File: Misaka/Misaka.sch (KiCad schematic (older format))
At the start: 4 parts, among them J1 Conn_Coaxial_Power, SW1 SW_DIP_x03, U2 ATmega2560-16AU

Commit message: CH340
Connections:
- net D1 renamed RX0
- net D18 renamed TX1
- net D19 renamed RX1
- net D2 renamed TX0
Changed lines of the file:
@@
 $Descr A4 11693 8268
 encoding utf-8
-Sheet 1 4
+Sheet 1 5
 Title ""
 Date ""
@@
 D50
 Text Label 5100 5300 0    50   ~ 0
-D1
+RX0
 Text Label 5100 5400 0    50   ~ 0
-D2
+TX0
 $Comp
 L Connector:Conn_Coaxial_Power J1
@@
 MS3
 $Comp
+L power:GND #PWR0127
+U 1 1 5E64EFCB
+P 7950 2750
+F 0 "#PWR0127" H 7950 2500 50  0001 C CNN
+F 1 "GND" H 7955 2577 50  0000 C CNN
+F 2 "" H 7950 2750 50  0001 C CNN
+F 3 "" H 7950 2750 50  0001 C CNN
+	1    7950 2750
+	1    0    0    -1
+$EndComp
+$Comp
+L power:+3.3V #PWR0142
+U 1 1 5E64FE9B
+P 8050 1300
+F 0 "#PWR0142" H 8050 1150 50  0001 C CNN
+F 1 "+3.3V" H 8065 1473 50  0000 C CNN
+F 2 "" H 8050 1300 50  0001 C CNN
+F 3 "" H 8050 1300 50  0001 C CNN
+	1    8050 1300
+	1    0    0    -1
+$EndComp
+Wire Wire Line
+	8050 1300 8050 1550
+Text Label 5100 4700 0    50   ~ 0
+TX1
+Text Label 5100 4600 0    50   ~ 0
+RX1
+Text Notes 8450 1000 2    50   ~ 0
+Connect with TX1/RX1
+$Sheet
+S 9800 550  1000 950
+U 5E609346
+F0 "USB-UART" 50
+F1 "CH340.sch" 50
+F2 "TX" I L 9800 1150 50
+F3 "RX" I L 9800 850 50
+$EndSheet
+Wire Wire Line
+	9800 850  9500 850
+Wire Wire Line
+	9800 1150 9500 1150
+Text Label 9500 850  0    50   ~ 0
+TX0
+Text Label 9500 1150 0    50   ~ 0
+RX0
+$Comp
 L dk_RF-Transceiver-Modules:XB24CZ7PIT-004 MOD1
 U 1 1 5E64862E
@@
 	1    0    0    -1
 $EndComp
-$Comp
-L power:GND #PWR0127
-U 1 1 5E64EFCB
-P 7950 2750
-F 0 "#PWR0127" H 7950 2500 50  0001 C CNN
-F 1 "GND" H 7955 2577 50  0000 C CNN
-F 2 "" H 7950 2750 50  0001 C CNN
-F 3 "" H 7950 2750 50  0001 C CNN
-	1    7950 2750
-	1    0    0    -1
-$EndComp
-$Comp
-L power:+3.3V #PWR0142
-U 1 1 5E64FE9B
-P 8050 1300
-F 0 "#PWR0142" H 8050 1150 50  0001 C CNN
-F 1 "+3.3V" H 8065 1473 50  0000 C CNN
-F 2 "" H 8050 1300 50  0001 C CNN
-F 3 "" H 8050 1300 50  0001 C CNN
-	1    8050 1300
-	1    0    0    -1
-$EndComp
-Wire Wire Line
-	8050 1300 8050 1550
-Text Label 5100 4700 0    50   ~ 0
-D18
-Text Label 5100 4600 0    50   ~ 0
-D19
+Text Label 7350 1750 2    50   ~ 0
+TX1
 Text Label 8750 1750 0    50   ~ 0
-D19
-Text Label 7350 1750 2    50   ~ 0
-D18
-Text Notes 8450 1000 2    50   ~ 0
-Connect with TX1/RX1
+RX1
 $EndSCHEMATC

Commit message: CH340C
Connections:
- net +5V: now also U2.100 (AVCC)
- net RESET: now reaches U2.30 (~RESET)
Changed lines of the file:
@@
 	4300 7200 4300 7450
 Wire Wire Line
-	4300 1400 4300 1300
+	4300 1400 4300 1350
 Wire Wire Line
 	9750 3150 9500 3150
@@
 Connect with TX1/RX1
 $Sheet
-S 9800 550  1000 950
+S 9750 550  1000 950
 U 5E609346
 F0 "USB-UART" 50
 F1 "CH340.sch" 50
-F2 "TX" I L 9800 1150 50
-F3 "RX" I L 9800 850 50
+F2 "TX" O L 9750 750 50
+F3 "RX" I L 9750 1250 50
+F4 "RESET" O L 9750 1000 50
 $EndSheet
 Wire Wire Line
-	9800 850  9500 850
-Wire Wire Line
-	9800 1150 9500 1150
-Text Label 9500 850  0    50   ~ 0
+	9750 750  9500 750
+Wire Wire Line
+	9750 1250 9500 1250
+Text Label 9500 750  0    50   ~ 0
 TX0
-Text Label 9500 1150 0    50   ~ 0
+Text Label 9500 1250 0    50   ~ 0
 RX0
 $Comp
@@
 Text Label 8750 1750 0    50   ~ 0
 RX1
+Wire Wire Line
+	9750 1000 9500 1000
+Text Label 9500 1000 0    50   ~ 0
+RESET
+Text Label 3500 1700 2    50   ~ 0
+RESET
+Wire Wire Line
+	4300 1350 4400 1350
+Wire Wire Line
+	4400 1350 4400 1400
+Connection ~ 4300 1350
+Wire Wire Line
+	4300 1350 4300 1300
 $EndSCHEMATC

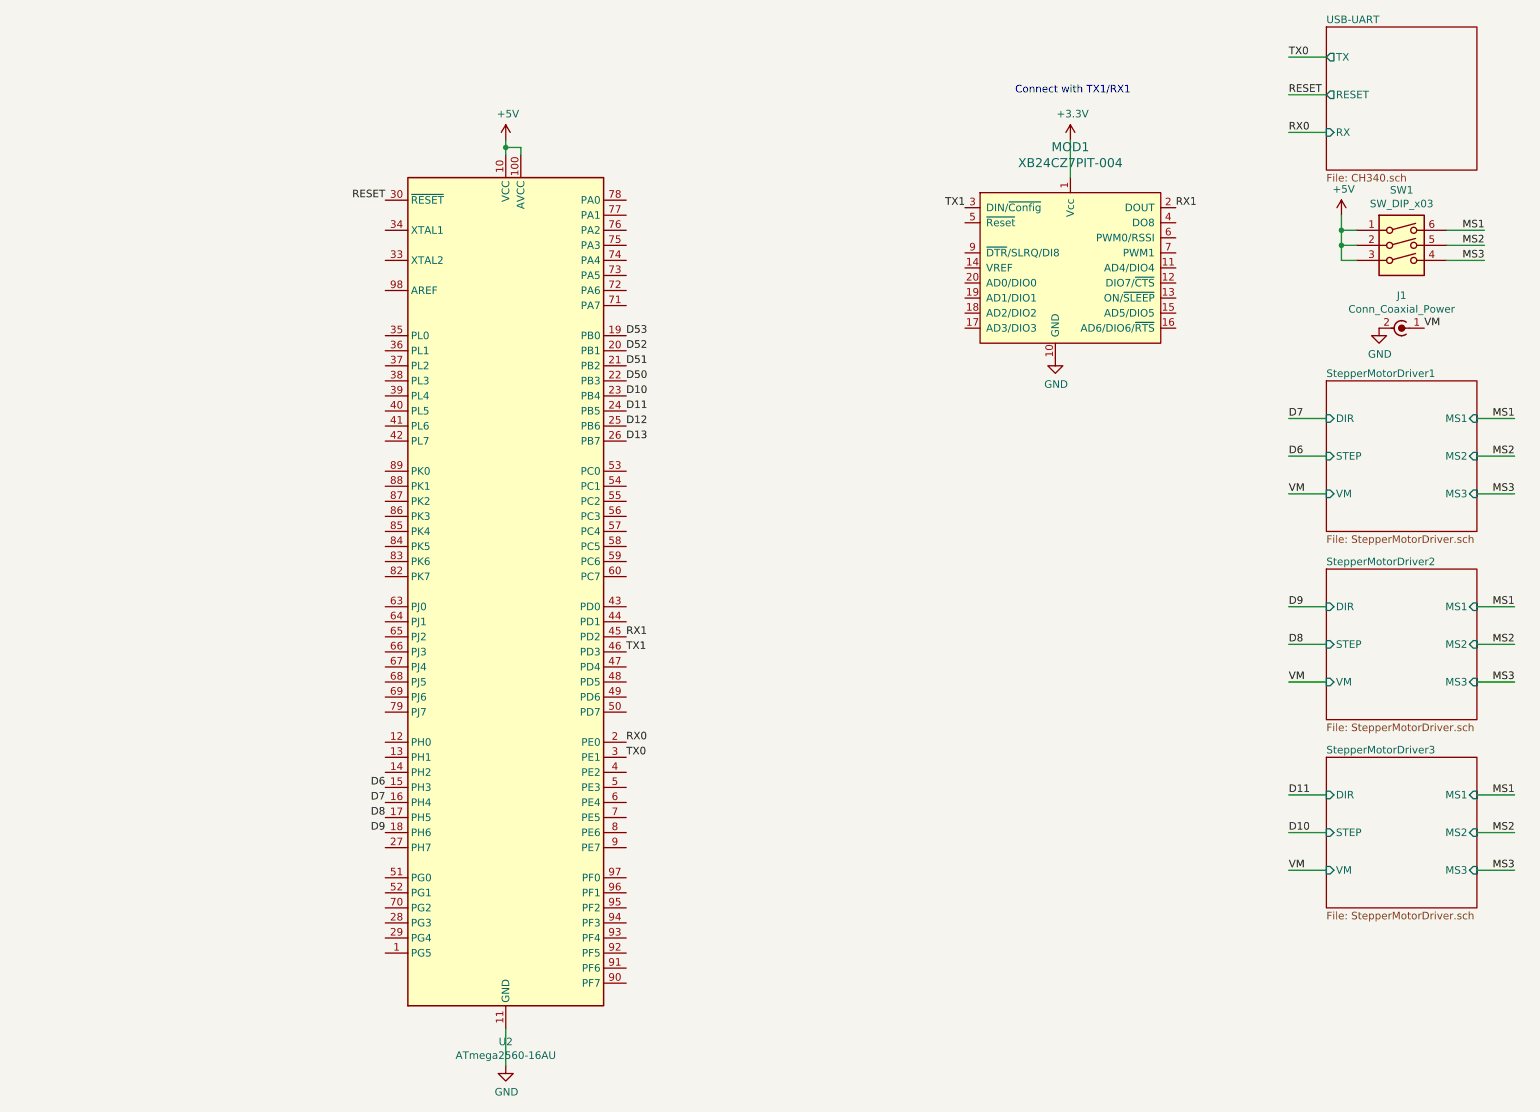
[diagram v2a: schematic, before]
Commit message: MURATA的 CSTLS16M0X51-A0
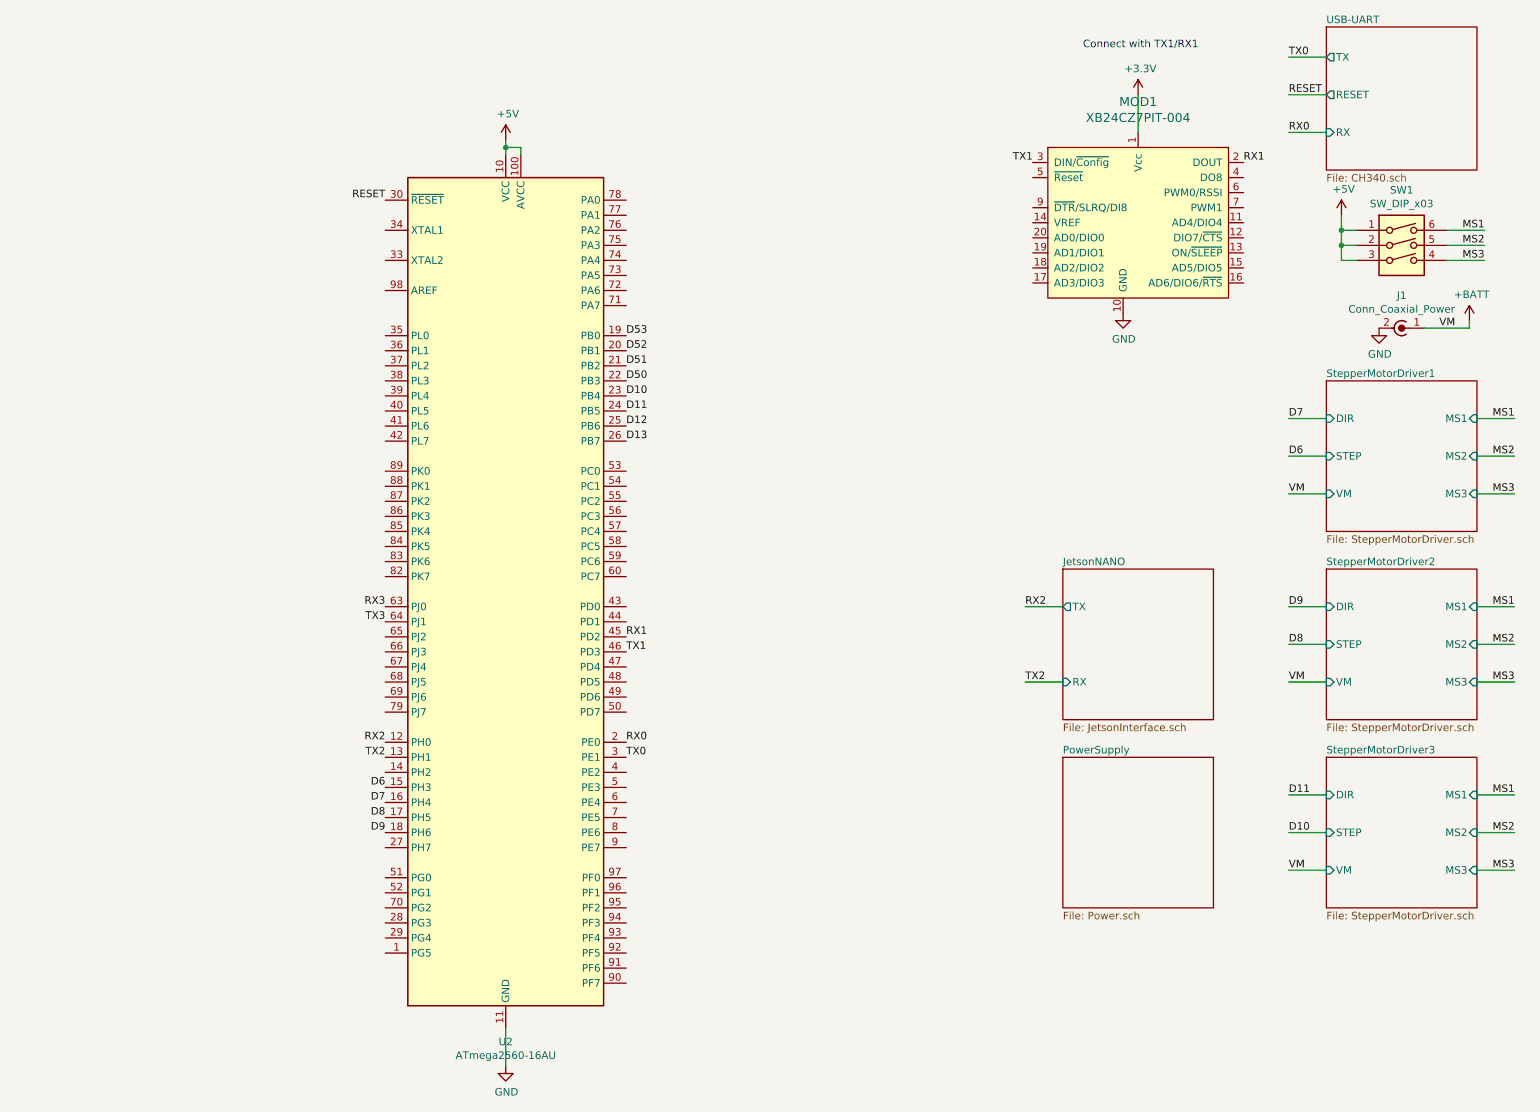
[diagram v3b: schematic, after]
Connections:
- net RX2: now reaches U2.12 (PH0)
- net TX2: now reaches U2.13 (PH1)
- net RX3: now reaches U2.63 (PJ0)
- net TX3: now reaches U2.64 (PJ1)
- net VM renamed +BATT
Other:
- moved on the sheet: MOD1
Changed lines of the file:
@@
 $Descr A4 11693 8268
 encoding utf-8
-Sheet 1 5
+Sheet 1 7
 Title ""
 Date ""
@@
 	0    1    1    0
 $EndComp
-Text Label 10400 2550 0    50   ~ 0
-VM
 $Comp
 L power:GND #PWR0117
@@
 L power:GND #PWR0127
 U 1 1 5E64EFCB
-P 7950 2750
-F 0 "#PWR0127" H 7950 2500 50  0001 C CNN
-F 1 "GND" H 7955 2577 50  0000 C CNN
-F 2 "" H 7950 2750 50  0001 C CNN
-F 3 "" H 7950 2750 50  0001 C CNN
-	1    7950 2750
+P 8400 2450
+F 0 "#PWR0127" H 8400 2200 50  0001 C CNN
+F 1 "GND" H 8405 2277 50  0000 C CNN
+F 2 "" H 8400 2450 50  0001 C CNN
+F 3 "" H 8400 2450 50  0001 C CNN
+	1    8400 2450
 	1    0    0    -1
 $EndComp
@@
 L power:+3.3V #PWR0142
 U 1 1 5E64FE9B
-P 8050 1300
-F 0 "#PWR0142" H 8050 1150 50  0001 C CNN
-F 1 "+3.3V" H 8065 1473 50  0000 C CNN
-F 2 "" H 8050 1300 50  0001 C CNN
-F 3 "" H 8050 1300 50  0001 C CNN
-	1    8050 1300
-	1    0    0    -1
-$EndComp
-Wire Wire Line
-	8050 1300 8050 1550
+P 8500 1000
+F 0 "#PWR0142" H 8500 850 50  0001 C CNN
+F 1 "+3.3V" H 8515 1173 50  0000 C CNN
+F 2 "" H 8500 1000 50  0001 C CNN
+F 3 "" H 8500 1000 50  0001 C CNN
+	1    8500 1000
+	1    0    0    -1
+$EndComp
+Wire Wire Line
+	8500 1000 8500 1250
 Text Label 5100 4700 0    50   ~ 0
 TX1
 Text Label 5100 4600 0    50   ~ 0
 RX1
-Text Notes 8450 1000 2    50   ~ 0
+Text Notes 8900 700  2    50   ~ 0
 Connect with TX1/RX1
+Wire Wire Line
+	9750 750  9500 750
+Wire Wire Line
+	9750 1250 9500 1250
+Text Label 9500 750  0    50   ~ 0
+TX0
+Text Label 9500 1250 0    50   ~ 0
+RX0
+$Comp
+L dk_RF-Transceiver-Modules:XB24CZ7PIT-004 MOD1
+U 1 1 5E64862E
+P 8600 2050
+F 0 "MOD1" H 8500 3053 60  0000 C CNN
+F 1 "XB24CZ7PIT-004" H 8500 2947 60  0000 C CNN
+F 2 "digikey-footprints:XBEE_PRO-20_THT" H 8800 2250 60  0001 L CNN
+F 3 "https://www.digi.com/resources/documentation/digidocs/pdfs/90001500.pdf" H 8800 2350 60  0001 L CNN
+F 4 "602-1557-ND" H 8800 2450 60  0001 L CNN "Digi-Key_PN"
+F 5 "XB24CZ7PIT-004" H 8800 2550 60  0001 L CNN "MPN"
+F 6 "RF/IF and RFID" H 8800 2650 60  0001 L CNN "Category"
+F 7 "RF Transceiver Modules" H 8800 2750 60  0001 L CNN "Family"
+F 8 "https://www.digi.com/resources/documentation/digidocs/pdfs/90001500.pdf" H 8800 2850 60  0001 L CNN "DK_Datasheet_Link"
+F 9 "/product-detail/en/digi-international/XB24CZ7PIT-004/602-1557-ND/5322371" H 8800 2950 60  0001 L CNN "DK_Detail_Page"
+F 10 "RF TXRX MOD 802.15.4 TRACE ANT" H 8800 3050 60  0001 L CNN "Description"
+F 11 "Digi International" H 8800 3150 60  0001 L CNN "Manufacturer"
+F 12 "Active" H 8800 3250 60  0001 L CNN "Status"
+	1    8600 2050
+	1    0    0    -1
+$EndComp
+Text Label 7800 1450 2    50   ~ 0
+TX1
+Text Label 9200 1450 0    50   ~ 0
+RX1
+Wire Wire Line
+	9750 1000 9500 1000
+Text Label 9500 1000 0    50   ~ 0
+RESET
+Text Label 3500 1700 2    50   ~ 0
+RESET
+Wire Wire Line
+	4300 1350 4400 1350
+Wire Wire Line
+	4400 1350 4400 1400
+Connection ~ 4300 1350
+Wire Wire Line
+	4300 1350 4300 1300
+$Sheet
+S 8000 5400 1000 1000
+U 5E6177DE
+F0 "PowerSupply" 50
+F1 "Power.sch" 50
+$EndSheet
+Text Label 3500 4400 2    50   ~ 0
+RX3
+Text Label 3500 4500 2    50   ~ 0
+TX3
+Text Label 3500 5300 2    50   ~ 0
+RX2
+Text Label 3500 5400 2    50   ~ 0
+TX2
+$Sheet
+S 8000 4150 1000 1000
+U 5E61980C
+F0 "JetsonNANO" 50
+F1 "JetsonInterface.sch" 50
+F2 "TX" O L 8000 4400 50
+F3 "RX" I L 8000 4900 50
+$EndSheet
+Wire Wire Line
+	8000 4400 7750 4400
+Wire Wire Line
+	8000 4900 7750 4900
+Text Label 7750 4400 0    50   ~ 0
+RX2
+Text Label 7750 4900 0    50   ~ 0
+TX2
+$Comp
+L power:+BATT #PWR?
+U 1 1 5E62480E
+P 10700 2500
+F 0 "#PWR?" H 10700 2350 50  0001 C CNN
+F 1 "+BATT" H 10715 2673 50  0000 C CNN
+F 2 "" H 10700 2500 50  0001 C CNN
+F 3 "" H 10700 2500 50  0001 C CNN
+	1    10700 2500
+	1    0    0    -1
+$EndComp
 $Sheet
 S 9750 550  1000 950
@@
 $EndSheet
 Wire Wire Line
-	9750 750  9500 750
-Wire Wire Line
-	9750 1250 9500 1250
-Text Label 9500 750  0    50   ~ 0
-TX0
-Text Label 9500 1250 0    50   ~ 0
-RX0
-$Comp
-L dk_RF-Transceiver-Modules:XB24CZ7PIT-004 MOD1
-U 1 1 5E64862E
-P 8150 2350
-F 0 "MOD1" H 8050 3353 60  0000 C CNN
-F 1 "XB24CZ7PIT-004" H 8050 3247 60  0000 C CNN
-F 2 "digikey-footprints:XBEE_PRO-20_THT" H 8350 2550 60  0001 L CNN
-F 3 "https://www.digi.com/resources/documentation/digidocs/pdfs/90001500.pdf" H 8350 2650 60  0001 L CNN
-F 4 "602-1557-ND" H 8350 2750 60  0001 L CNN "Digi-Key_PN"
-F 5 "XB24CZ7PIT-004" H 8350 2850 60  0001 L CNN "MPN"
-F 6 "RF/IF and RFID" H 8350 2950 60  0001 L CNN "Category"
-F 7 "RF Transceiver Modules" H 8350 3050 60  0001 L CNN "Family"
-F 8 "https://www.digi.com/resources/documentation/digidocs/pdfs/90001500.pdf" H 8350 3150 60  0001 L CNN "DK_Datasheet_Link"
-F 9 "/product-detail/en/digi-international/XB24CZ7PIT-004/602-1557-ND/5322371" H 8350 3250 60  0001 L CNN "DK_Detail_Page"
-F 10 "RF TXRX MOD 802.15.4 TRACE ANT" H 8350 3350 60  0001 L CNN "Description"
-F 11 "Digi International" H 8350 3450 60  0001 L CNN "Manufacturer"
-F 12 "Active" H 8350 3550 60  0001 L CNN "Status"
-	1    8150 2350
-	1    0    0    -1
-$EndComp
-Text Label 7350 1750 2    50   ~ 0
-TX1
-Text Label 8750 1750 0    50   ~ 0
-RX1
-Wire Wire Line
-	9750 1000 9500 1000
-Text Label 9500 1000 0    50   ~ 0
-RESET
-Text Label 3500 1700 2    50   ~ 0
-RESET
-Wire Wire Line
-	4300 1350 4400 1350
-Wire Wire Line
-	4400 1350 4400 1400
-Connection ~ 4300 1350
-Wire Wire Line
-	4300 1350 4300 1300
+	10400 2550 10700 2550
+Wire Wire Line
+	10700 2550 10700 2500
+Text Label 10500 2550 0    50   ~ 0
+VM
 $EndSCHEMATC

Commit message: V1
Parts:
- added ICSP1: Conn_02x03_Odd_Even, Connector_PinHeader_2.54mm:PinHeader_2x03_P2.54mm_Vertical, symbol Connector_Generic:Conn_02x03_Odd_Even
- added R26: 1M, Resistor_SMD:R_0603_1608Metric_Pad1.05x0.95mm_HandSolder, symbol Device:R
- added Y1: CSTLS16M0X51-B0, Crystal:Resonator_muRata_CSTLSxxxX-3Pin_W5.5mm_H3.0mm, symbol SparkFun-Clocks:RESONATOR-16MHZSMD_3.2X1.3
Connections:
- net +5V: now also ICSP1.2 (Pin_2)
- net GND: now also ICSP1.6 (Pin_6), Y1.2
- net RESET: now also ICSP1.5 (Pin_5)
- net TX1: no longer MOD1.3 (DIN/~Config)
- net at U2.33 (XTAL2): now also R26.2, Y1.3
- net at U2.34 (XTAL1): now also R26.1, Y1.1
- net SCL: now reaches U2.43 (PD0)
- net SDA: now reaches U2.44 (PD1)
- net D3: now reaches U2.7 (PE5)
- net D50 renamed MISO
- net MISO: now also ICSP1.1 (Pin_1)
- net D51 renamed MOSI
- net MOSI: now also ICSP1.4 (Pin_4)
- net D52 renamed SCK
- net SCK: now also ICSP1.3 (Pin_3)
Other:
- moved on the sheet: J1, SW1, U2

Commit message: route v1.1
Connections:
- net TX1: now also MOD1.3 (DIN/~Config)
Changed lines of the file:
@@
 Text Label 6300 3650 0    50   ~ 0
 D13
+Text Label 7800 1450 2    50   ~ 0
+TX1
 $EndSCHEMATC

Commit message: 电池正负极反了
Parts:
- J1: value Conn_Coaxial_Power -> Battery; symbol Connector:Conn_Coaxial_Power -> Device:Battery_Cell
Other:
- note added: "AMASS package and this symbol \npositive and negative mapping is opposite\nIt can be corrected by welding on the reverse side\nwhen soldering, or you can directly connect the positive \nelectrode of the symbol to GND for violent correction."
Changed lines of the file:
@@
 Text Label 5800 4800 0    50   ~ 0
 TX0
-$Comp
-L Connector:Conn_Coaxial_Power J1
-U 1 1 5E620D8E
-P 10000 2550
-F 0 "J1" V 9783 2500 50  0000 C CNN
-F 1 "Conn_Coaxial_Power" V 9874 2500 50  0000 C CNN
-F 2 "Connector_AMASS:AMASS_XT30PW-M_1x02_P2.50mm_Horizontal" H 10000 2500 50  0001 C CNN
-F 3 "~" H 10000 2500 50  0001 C CNN
-	1    10000 2550
-	0    1    1    0
-$EndComp
-$Comp
-L power:GND #PWR0117
-U 1 1 5E622AF8
-P 9800 2550
-F 0 "#PWR0117" H 9800 2300 50  0001 C CNN
-F 1 "GND" H 9805 2377 50  0000 C CNN
-F 2 "" H 9800 2550 50  0001 C CNN
-F 3 "" H 9800 2550 50  0001 C CNN
-	1    9800 2550
-	1    0    0    -1
-$EndComp
 Wire Wire Line
 	10450 3150 10700 3150
@@
 Text Label 7850 2400 2    50   ~ 0
 TX1
-Text Label 9200 1450 0    50   ~ 0
-RX1
 Wire Wire Line
 	6500 5900 6250 5900
@@
 Text Label 7750 4900 0    50   ~ 0
 TX2
-$Comp
-L power:+BATT #PWR0152
-U 1 1 5E62480E
-P 10400 2500
-F 0 "#PWR0152" H 10400 2350 50  0001 C CNN
-F 1 "+BATT" H 10415 2673 50  0000 C CNN
-F 2 "" H 10400 2500 50  0001 C CNN
-F 3 "" H 10400 2500 50  0001 C CNN
-	1    10400 2500
-	1    0    0    -1
-$EndComp
-Wire Wire Line
-	10100 2550 10400 2550
-Wire Wire Line
-	10400 2550 10400 2500
-Text Label 10200 2550 0    50   ~ 0
-VM
 $Comp
 L SparkFun-Clocks:RESONATOR-16MHZSMD_3.2X1.3 Y1
@@
 F4 "RESET" O L 6500 5900 50
 $EndSheet
+Wire Wire Line
+	1700 2650 2100 2650
+Wire Wire Line
+	1400 2650 1300 2650
+$Comp
+L power:GND #PWR0117
+U 1 1 5E622AF8
+P 1300 2650
+F 0 "#PWR0117" H 1300 2400 50  0001 C CNN
+F 1 "GND" H 1305 2477 50  0000 C CNN
+F 2 "" H 1300 2650 50  0001 C CNN
+F 3 "" H 1300 2650 50  0001 C CNN
+	1    1300 2650
+	1    0    0    -1
+$EndComp
+Text Label 1900 2650 0    50   ~ 0
+VM
+Wire Wire Line
+	2100 2650 2100 2600
+$Comp
+L power:+BATT #PWR0152
+U 1 1 5E62480E
+P 2100 2600
+F 0 "#PWR0152" H 2100 2450 50  0001 C CNN
+F 1 "+BATT" H 2115 2773 50  0000 C CNN
+F 2 "" H 2100 2600 50  0001 C CNN
+F 3 "" H 2100 2600 50  0001 C CNN
+	1    2100 2600
+	1    0    0    -1
+$EndComp
+Text Label 9200 1450 0    50   ~ 0
+RX1
+Text Notes 1200 3400 0    50   ~ 0
+AMASS package and this symbol \npositive and negative mapping is opposite\nIt can be corrected by welding on the reverse side\nwhen soldering, or you can directly connect the positive \nelectrode of the symbol to GND for violent correction.
+$Comp
+L Device:Battery_Cell J1
+U 1 1 5E620D8E
+P 1500 2650
+F 0 "J1" V 1283 2600 50  0000 C CNN
+F 1 "Battery" V 1374 2600 50  0000 C CNN
+F 2 "Connector_AMASS:AMASS_XT30PW-M_1x02_P2.50mm_Horizontal" V 1150 3550 50  0000 C CNN
+F 3 "~" H 1500 2600 50  0001 C CNN
+	1    1500 2650
+	0    1    1    0
+$EndComp
 $EndSCHEMATC
